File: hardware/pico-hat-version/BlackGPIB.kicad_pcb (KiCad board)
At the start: 2 copper layers, 7 parts, among them J1 SD_Card_Module, J2 Raspberry_Pi_Connector

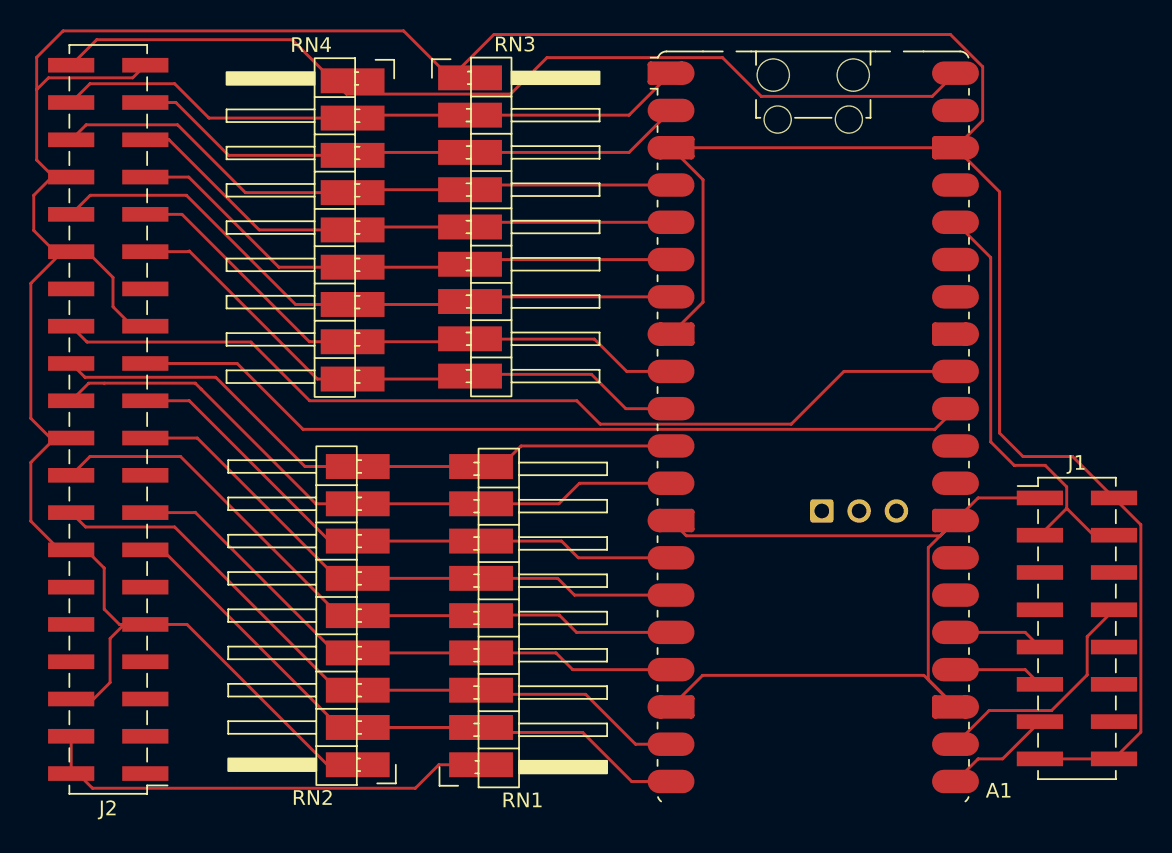
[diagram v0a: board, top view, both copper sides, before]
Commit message: fix voltage divider for pico hat hardware
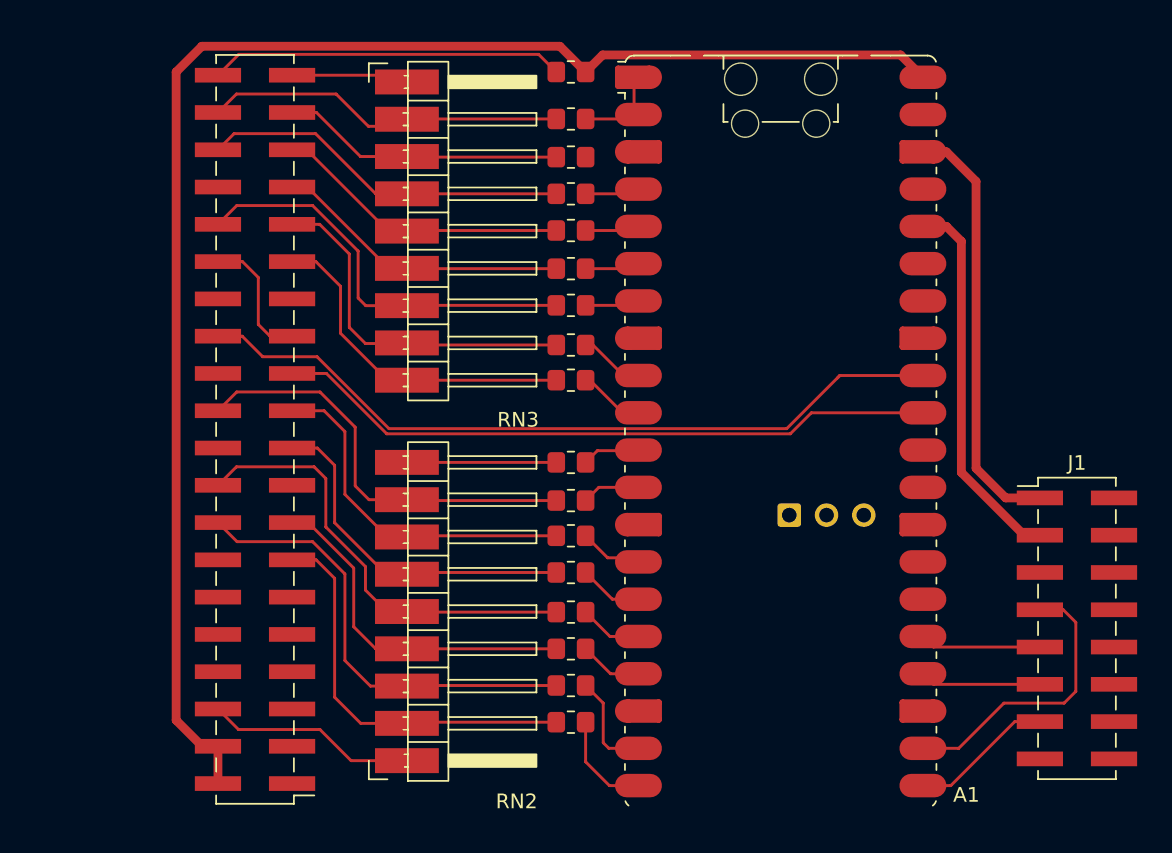
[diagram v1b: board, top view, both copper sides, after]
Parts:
- removed RN1, RN4: 3K3, custom:PinHeader_1x09_P2.54mm_Horizontal_Left
- added R1: 3K3, Resistor_SMD:R_0805_2012Metric_Pad1.20x1.40mm_HandSolder, F.Cu at (173.0, 29.2)
- added R10: 3K3, Resistor_SMD:R_0805_2012Metric_Pad1.20x1.40mm_HandSolder, F.Cu at (173.0, 55.2)
- added R11: 3K3, Resistor_SMD:R_0805_2012Metric_Pad1.20x1.40mm_HandSolder, F.Cu at (173.0, 57.6)
- added R12: 3K3, Resistor_SMD:R_0805_2012Metric_Pad1.20x1.40mm_HandSolder, F.Cu at (173.0, 60.1)
- added R13: 3K3, Resistor_SMD:R_0805_2012Metric_Pad1.20x1.40mm_HandSolder, F.Cu at (173.0, 62.8)
- added R14: 3K3, Resistor_SMD:R_0805_2012Metric_Pad1.20x1.40mm_HandSolder, F.Cu at (173.0, 65.3)
- added R15: 3K3, Resistor_SMD:R_0805_2012Metric_Pad1.20x1.40mm_HandSolder, F.Cu at (173.0, 67.8)
- added R16: 3K3, Resistor_SMD:R_0805_2012Metric_Pad1.20x1.40mm_HandSolder, F.Cu at (173.0, 70.3)
- added R17: 1K, Resistor_SMD:R_0805_2012Metric_Pad1.20x1.40mm_HandSolder, F.Cu at (173.0, 26.0)
- added R2: 3K3, Resistor_SMD:R_0805_2012Metric_Pad1.20x1.40mm_HandSolder, F.Cu at (173.0, 31.8)
- added R3: 3K3, Resistor_SMD:R_0805_2012Metric_Pad1.20x1.40mm_HandSolder, F.Cu at (173.0, 34.3)
- added R4: 3K3, Resistor_SMD:R_0805_2012Metric_Pad1.20x1.40mm_HandSolder, F.Cu at (173.0, 36.8)
- added R5: 3K3, Resistor_SMD:R_0805_2012Metric_Pad1.20x1.40mm_HandSolder, F.Cu at (173.0, 39.4)
- added R6: 3K3, Resistor_SMD:R_0805_2012Metric_Pad1.20x1.40mm_HandSolder, F.Cu at (173.0, 41.9)
- added R7: 3K3, Resistor_SMD:R_0805_2012Metric_Pad1.20x1.40mm_HandSolder, F.Cu at (173.0, 44.6)
- added R8: 3K3, Resistor_SMD:R_0805_2012Metric_Pad1.20x1.40mm_HandSolder, F.Cu at (173.0, 47.0)
- added R9: 3K3, Resistor_SMD:R_0805_2012Metric_Pad1.20x1.40mm_HandSolder, F.Cu at (173.0, 52.6)
- RN2: footprint custom:PinHeader_1x09_P2.54mm_Horizontal_Right -> custom:PinHeader_1x09_P2.54mm_Horizontal_Right_FlipX
- moved RN2 20.6 mm to (160.5, 52.6), turned to 0 degrees
- moved J2 10.0 mm to (151.5, 50.4)
- moved RN3 4.31 mm to (160.5, 26.7)
- moved A1 2.24 mm to (187.3, 50.5)
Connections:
- A1 pad 1: GPIB_DIO8 -> Net-(A1-GPIO0)
- A1 pad 10: GPIB_DIO1 -> Net-(A1-GPIO7)
- A1 pad 11: GPIB_SRQ -> Net-(A1-GPIO8)
- A1 pad 12: GPIB_EOI -> Net-(A1-GPIO9)
- A1 pad 14: GPIB_ATN -> Net-(A1-GPIO10)
- A1 pad 15: GPIB_DAV -> Net-(A1-GPIO11)
- A1 pad 16: GPIB_NRFD -> Net-(A1-GPIO12)
- A1 pad 17: GPIB_NDAC -> Net-(A1-GPIO13)
- A1 pad 19: GPIB_IFC -> Net-(A1-GPIO14)
- A1 pad 2: GPIB_DIO7 -> Net-(A1-GPIO1)
- A1 pad 20: GPIB_REN -> Net-(A1-GPIO15)
- A1 pad 4: GPIB_DIO6 -> Net-(A1-GPIO2)
- A1 pad 5: GPIB_DIO5 -> Net-(A1-GPIO3)
- A1 pad 6: GPIB_DIO4 -> Net-(A1-GPIO4)
- A1 pad 7: GPIB_DIO3 -> Net-(A1-GPIO5)
- A1 pad 9: GPIB_DIO2 -> Net-(A1-GPIO6)
- J2 pad 40: +5V -> GPIB_PE
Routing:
- net GND: track 325.0 -> 58.8 mm
- net GPIB_SRQ: track 44.4 -> 11.5 mm
- net GPIB_PE: track 0.00 -> 24.1 mm
- net GPIB_DIO7: track 38.6 -> 19.3 mm
- net GPIB_DIO8: track 43.6 -> 24.7 mm
- net GPIB_DIO5: track 38.6 -> 20.3 mm
- net GPIB_DIO4: track 38.6 -> 20.3 mm
- net GPIB_DIO6: track 43.4 -> 25.2 mm
- net GPIB_DIO1: track 40.6 -> 23.2 mm
- net GPIB_DIO3: track 44.7 -> 28.3 mm
- net GPIB_NDAC: track 40.3 -> 23.9 mm
- net GPIB_EOI: track 45.4 -> 29.0 mm
- net GPIB_DAV: track 40.3 -> 23.9 mm
- net GPIB_IFC: track 47.4 -> 31.1 mm
- net GPIB_ATN: track 40.3 -> 24.1 mm
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
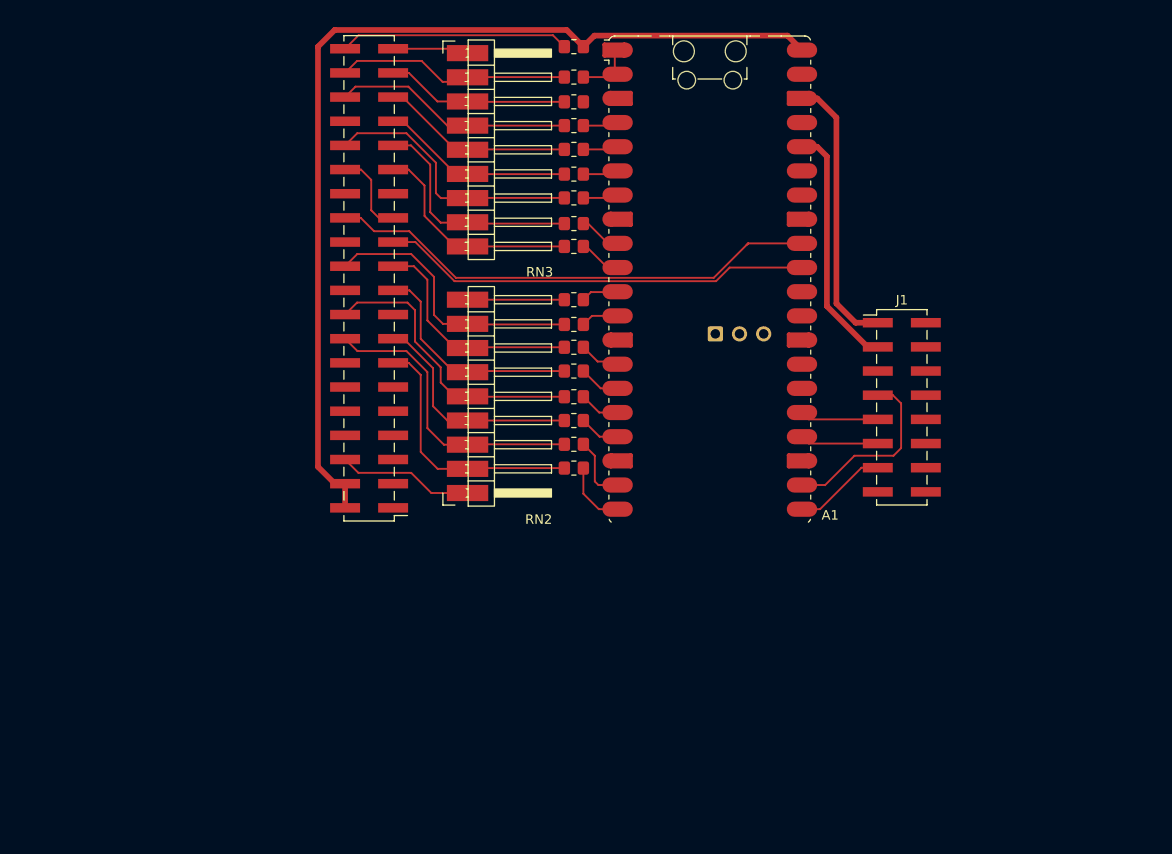
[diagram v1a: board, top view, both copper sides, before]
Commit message: pico: optimize hatted version for SLA printer, remove optional components
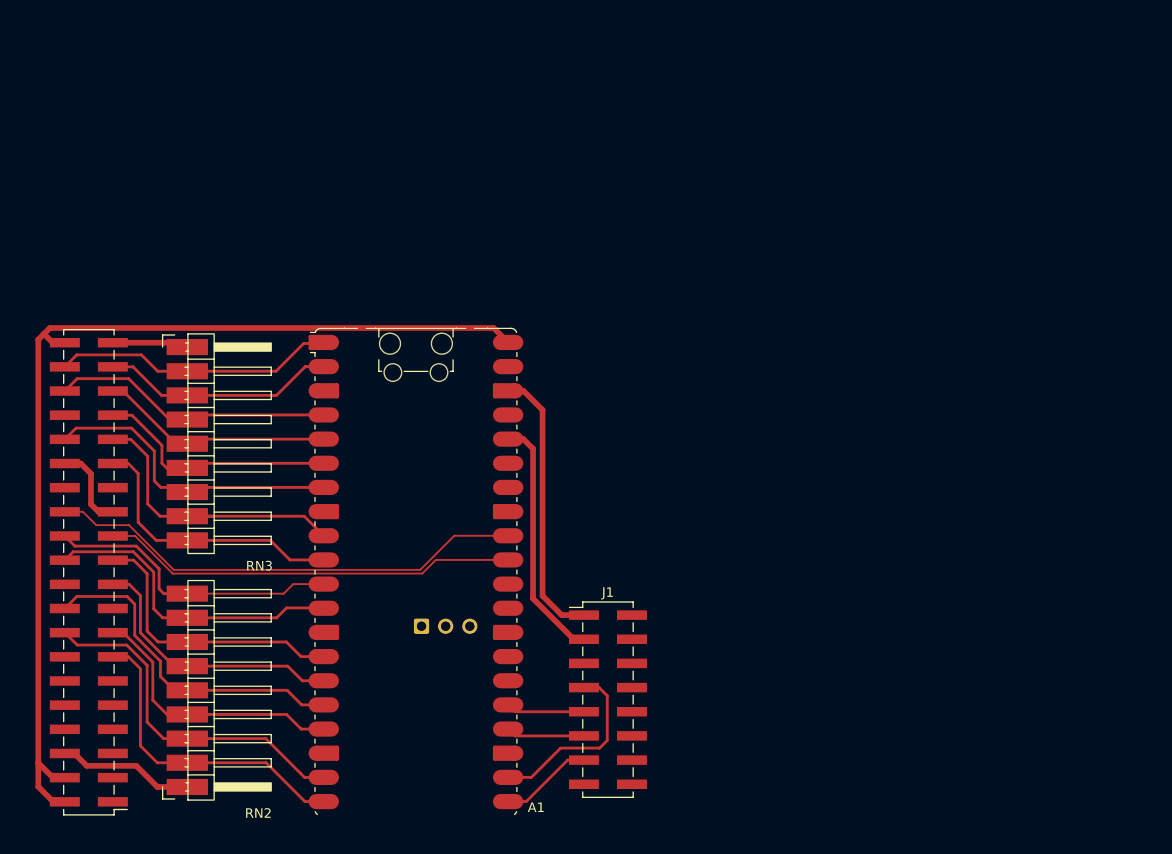
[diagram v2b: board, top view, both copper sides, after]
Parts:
- removed R1, R10, R11, R12, R13, R14, R15, R16, R2, R3, R4, R5, R6, R7, R8, R9: 3K3, Resistor_SMD:R_0805_2012Metric_Pad1.20x1.40mm_HandSolder
- removed R17: 1K, Resistor_SMD:R_0805_2012Metric_Pad1.20x1.40mm_HandSolder
- moved J1 43.6 mm to (176.6, 94.6)
- moved A1 43.6 mm to (156.4, 81.2)
- moved RN2 42.7 mm to (131.0, 83.5)
- moved RN3 42.7 mm to (131.0, 57.6)
- moved J2 42.7 mm to (122.0, 81.2)
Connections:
- A1 pad 1: Net-(A1-GPIO0) -> GPIB_DIO8
- A1 pad 10: Net-(A1-GPIO7) -> GPIB_DIO1
- A1 pad 11: Net-(A1-GPIO8) -> GPIB_SRQ
- A1 pad 12: Net-(A1-GPIO9) -> GPIB_EOI
- A1 pad 14: Net-(A1-GPIO10) -> GPIB_ATN
- A1 pad 15: Net-(A1-GPIO11) -> GPIB_DAV
- A1 pad 16: Net-(A1-GPIO12) -> GPIB_NRFD
- A1 pad 17: Net-(A1-GPIO13) -> GPIB_NDAC
- A1 pad 19: Net-(A1-GPIO14) -> GPIB_IFC
- A1 pad 2: Net-(A1-GPIO1) -> GPIB_DIO7
- A1 pad 20: Net-(A1-GPIO15) -> GPIB_REN
- A1 pad 4: Net-(A1-GPIO2) -> GPIB_DIO6
- A1 pad 40: +5V -> GPIB_PE
- A1 pad 5: Net-(A1-GPIO3) -> GPIB_DIO5
- A1 pad 6: Net-(A1-GPIO4) -> GPIB_DIO4
- A1 pad 7: Net-(A1-GPIO5) -> GPIB_DIO3
- A1 pad 9: Net-(A1-GPIO6) -> GPIB_DIO2
- J2 pad 2: +5V -> GPIB_PE
- J2 pad 4: +5V -> GPIB_PE
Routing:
- net +5V: track 103.7 -> 0.00 mm
- net GPIB_PE: track 24.1 -> 107.0 mm
- net GPIB_SRQ: track 11.5 -> 31.4 mm
- net GPIB_DIO2: track 24.4 -> 33.2 mm
- net GPIB_DIO1: track 23.2 -> 30.5 mm
- net Net-(A1-GPIO15): track 6.97 -> 0.00 mm
- net Net-(A1-GPIO14): track 6.95 -> 0.00 mm
- net GPIB_DIO4: track 20.3 -> 26.8 mm
- net Net-(A1-GPIO0): track 6.05 -> 0.00 mm
- net GPIB_REN: track 27.4 -> 33.3 mm
- net GPIB_IFC: track 31.1 -> 37.1 mm
- net GPIB_ATN: track 24.1 -> 30.0 mm
- net GPIB_DIO7: track 19.3 -> 24.7 mm
- net GPIB_DIO6: track 25.2 -> 30.6 mm
- net GPIB_DIO5: track 20.3 -> 25.5 mm
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
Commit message: pico: add ground polygon and improve traces in hatted version
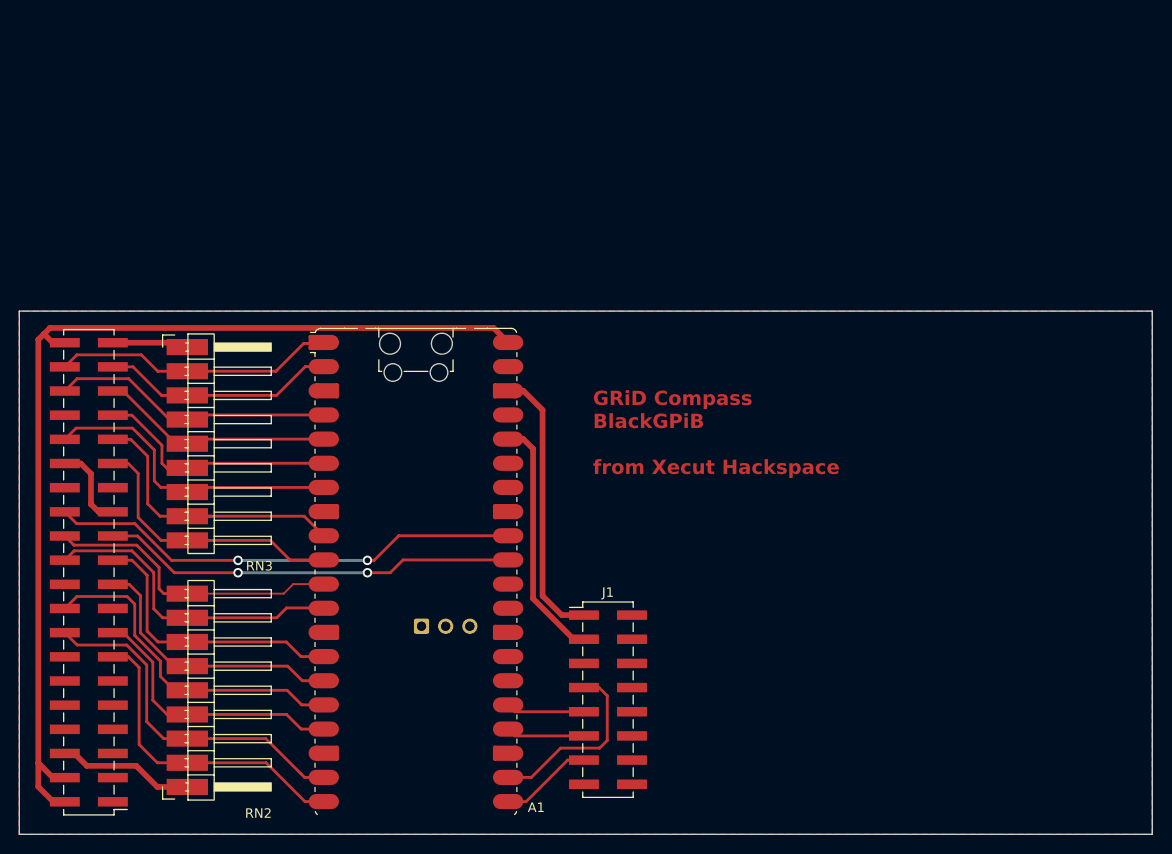
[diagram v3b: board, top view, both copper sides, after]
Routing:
- net GPIB_TE: track 50.6 -> 49.8 mm, vias 0 -> 2
- net GPIB_DC: track 43.8 -> 43.7 mm, vias 0 -> 2
- added copper zone on F.Cu, net GND
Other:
- board outline added: 119.1 x 55 mm
- board text added: "GRiD Compass BlackGPiB from Xecut Hackspace"
